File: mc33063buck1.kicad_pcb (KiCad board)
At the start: 2 copper layers, 78.4 x 45.5 mm, 30 parts, among them J1 Conn_01x01, J2 Conn_01x01, J3 Conn_01x01, J4 USB_A, J5 Jack-DC, Q1 MJE3055T, U1 MC34063

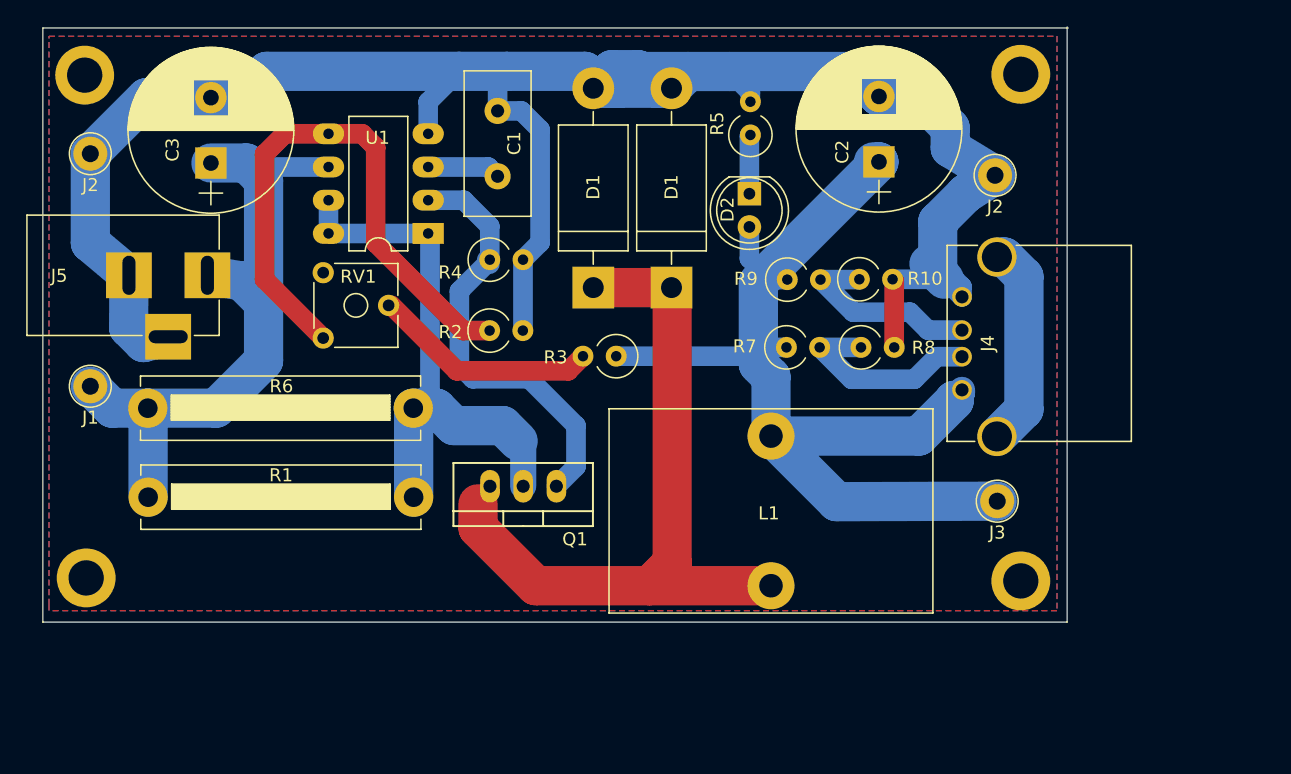
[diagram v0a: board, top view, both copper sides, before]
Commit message: fix resistor size and lines.
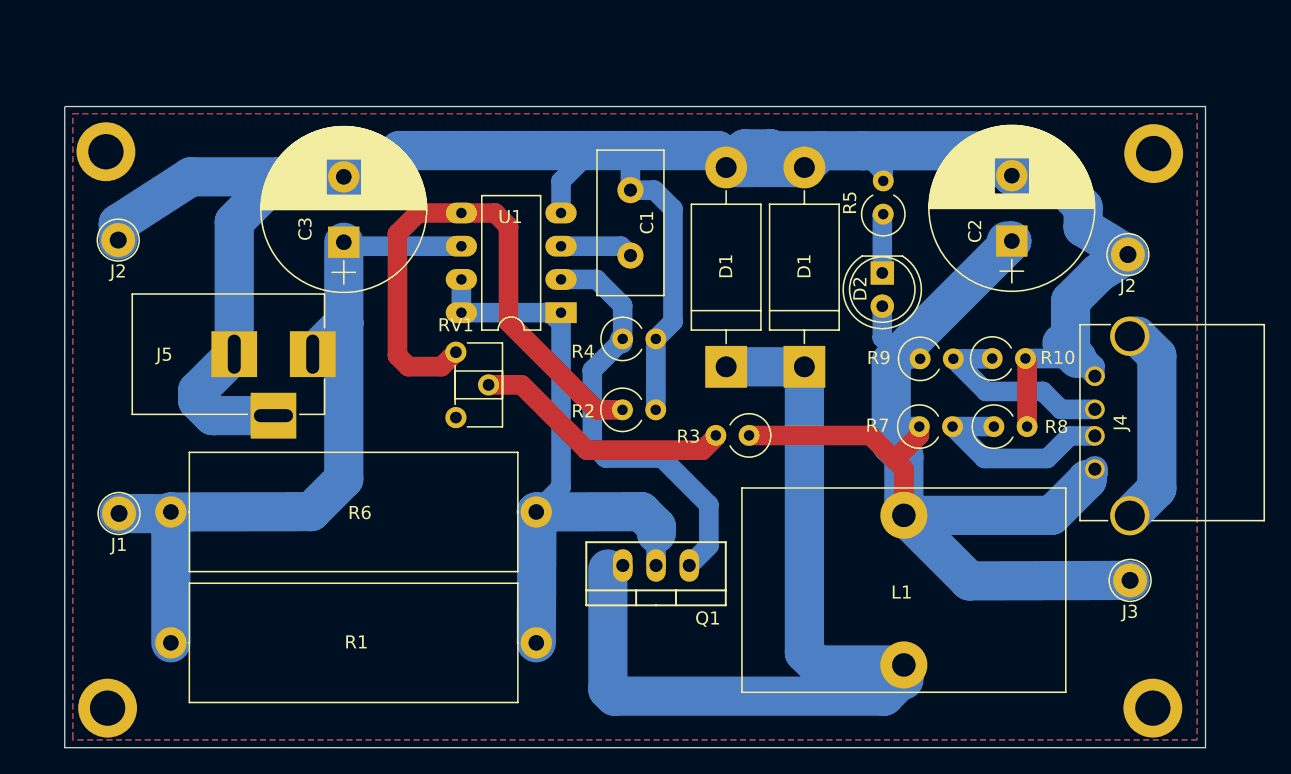
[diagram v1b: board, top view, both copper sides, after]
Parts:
- R1, R6: footprint Resistors_THT:R_Bare_Metal_Element_L21.3mm_W4.8mm_P20.30mm -> Resistors_THT:R_Axial_Power_L25.0mm_W9.0mm_P27.94mm
- RV1: footprint Potentiometers:Potentiometer_Trimmer_ACP_CA6v_Horizontal -> Potentiometers:Potentiometer_Trimmer_ACP_CA6h_Vertical
- moved REF** 14.0 mm to (97.9, 64.9)
- moved J2 11.8 mm to (96.0, 30.2)
- moved L1 11.8 mm to (78.9, 61.6)
- moved R10 11.8 mm to (85.7, 38.2)
- moved R7 11.8 mm to (80.1, 43.4)
- moved R2 11.8 mm to (57.4, 42.1)
- moved R4 11.8 mm to (57.4, 36.7)
- moved C1 11.8 mm to (58.0, 30.3)
- moved C3 11.8 mm to (36.1, 29.3)
- moved D1 11.8 mm to (65.3, 38.8)
- moved R3 11.8 mm to (67.1, 44.0)
- moved U1 11.8 mm to (52.7, 34.7)
- moved C2 11.8 mm to (87.2, 29.2)
- moved D2 11.8 mm to (77.3, 31.6)
- moved R5 11.8 mm to (77.3, 27.1)
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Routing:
- net GND: track 170.6 -> 186.9 mm
- net Net-(D1-Pad1): track 57.3 -> 70.9 mm
- net +5V: track 81.4 -> 90.1 mm
- net Net-(Q1-Pad2): track 43.6 -> 49.6 mm
- net +BATT: track 54.8 -> 59.1 mm
- net Net-(R3-Pad2): track 17.4 -> 20.0 mm
- net Net-(R2-Pad1): track 44.3 -> 43.0 mm
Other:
- board size 78.4 x 45.5 mm -> 87.2 x 49 mm

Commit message: update.
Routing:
- net Net-(D1-Pad1): track 70.9 -> 71.5 mm
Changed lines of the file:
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@@
-(kicad_pcb (version 4) (host pcbnew 4.0.7)
+(kicad_pcb (version 20171130) (host pcbnew "(5.0.0)")
   (general
-    (links 47)
-    (no_connects 0)
-    (area 1.837157 18.127 114.063043 69.222)
     (thickness 1.6)
     (drawings 4)
-    (tracks 173)
+    (tracks 176)
     (zones 0)
     (modules 30)
@@
   )
   (setup
-    (last_trace_width 1.5)
+    (last_trace_width 0.25)
     (user_trace_width 1.5)
     (user_trace_width 2)
@@
     (visible_elements 7FFFFFFF)
     (pcbplotparams
-      (layerselection 0x010f0_80000001)
+      (layerselection 0x010f0_ffffffff)
       (usegerberextensions false)
       (usegerberattributes true)
+      (usegerberadvancedattributes false)
+      (creategerberjobfile false)
       (excludeedgelayer false)
       (linewidth 0.150000)
@@
       (hpglpennumber 1)
       (hpglpenspeed 20)
-      (hpglpendiameter 15)
-      (hpglpenoverlay 2)
+      (hpglpendiameter 15.000000)
       (psnegative false)
       (psa4output false)
@@
       (net 9 "Net-(J4-Pad5)"))
     (model ${KISYS3DMOD}/Connectors.3dshapes/USB_A.wrl
-      (at (xyz 0.14 0 0))
+      (offset (xyz 3.555999946594238 0 0))
       (scale (xyz 1 1 1))
       (rotate (xyz 0 0 90))
@@
   (segment (start 45.0723 29.5783) (end 36.3855 29.5783) (width 1.5) (layer B.Cu) (net 4))
   (segment (start 36.3855 29.5783) (end 36.0807 29.2735) (width 1.5) (layer B.Cu) (net 4))
-  (segment (start 78.9051 61.595) (end 78.9051 62.4713) (width 3) (layer B.Cu) (net 5))
-  (segment (start 78.9051 62.4713) (end 77.3938 63.9826) (width 3) (layer B.Cu) (net 5))
-  (segment (start 56.2737 63.4746) (end 56.2737 54.2544) (width 3) (layer B.Cu) (net 5))
-  (segment (start 56.7817 63.9826) (end 56.2737 63.4746) (width 3) (layer B.Cu) (net 5))
-  (segment (start 77.3938 63.9826) (end 56.7817 63.9826) (width 3) (layer B.Cu) (net 5))
-  (segment (start 78.9051 61.595) (end 78.9051 62.7507) (width 3) (layer B.Cu) (net 5))
-  (segment (start 71.2978 38.7985) (end 71.2978 60.6425) (width 3) (layer B.Cu) (net 5))
-  (segment (start 72.2503 61.595) (end 78.9051 61.595) (width 3) (layer B.Cu) (net 5))
-  (segment (start 71.2978 60.6425) (end 72.2503 61.595) (width 3) (layer B.Cu) (net 5))
   (segment (start 71.2978 38.7985) (end 71.2978 38.8366) (width 3) (layer B.Cu) (net 5))
   (segment (start 57.4167 53.9877) (end 57.4167 54.3052) (width 1.5) (layer B.Cu) (net 5))
   (segment (start 65.3161 38.7985) (end 71.2978 38.7985) (width 3) (layer B.Cu) (net 5))
+  (segment (start 56.2737 63.4746) (end 56.2737 54.2544) (width 3) (layer B.Cu) (net 5))
+  (segment (start 56.261 64.7573) (end 56.2737 63.4746) (width 3) (layer B.Cu) (net 5))
+  (segment (start 78.9051 61.595) (end 78.9051 62.4713) (width 3) (layer B.Cu) (net 5))
+  (segment (start 77.105101 63.394999) (end 77.105101 63.788699) (width 3) (layer B.Cu) (net 5))
+  (segment (start 78.9051 61.595) (end 77.105101 63.394999) (width 3) (layer B.Cu) (net 5))
+  (segment (start 76.1365 64.7573) (end 56.261 64.7573) (width 3) (layer B.Cu) (net 5))
+  (segment (start 77.105101 63.788699) (end 76.1365 64.7573) (width 3) (layer B.Cu) (net 5))
+  (segment (start 76.359516 61.595) (end 76.270616 61.5061) (width 3) (layer B.Cu) (net 5))
+  (segment (start 78.9051 61.595) (end 76.359516 61.595) (width 3) (layer B.Cu) (net 5))
+  (segment (start 76.270616 61.5061) (end 72.5678 61.5061) (width 3) (layer B.Cu) (net 5))
+  (segment (start 71.2978 60.2361) (end 71.2978 38.7985) (width 3) (layer B.Cu) (net 5))
+  (segment (start 72.5678 61.5061) (end 71.2978 60.2361) (width 3) (layer B.Cu) (net 5))
   (segment (start 77.2541 31.623) (end 77.2541 27.2034) (width 1.5) (layer B.Cu) (net 6))
   (segment (start 77.2541 27.2034) (end 77.3303 27.1272) (width 1.5) (layer B.Cu) (net 6))
